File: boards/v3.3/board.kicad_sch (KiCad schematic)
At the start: 61 parts, among them J1 KF301-2P, J2 KF301-2P, J3 KF301-2P, J4 KF301-2P, J5 KF301-2P, J6 KF301-2P, P1 Pin Header, P2 Pin Header, P3 Pin Header, P4 Pin Header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

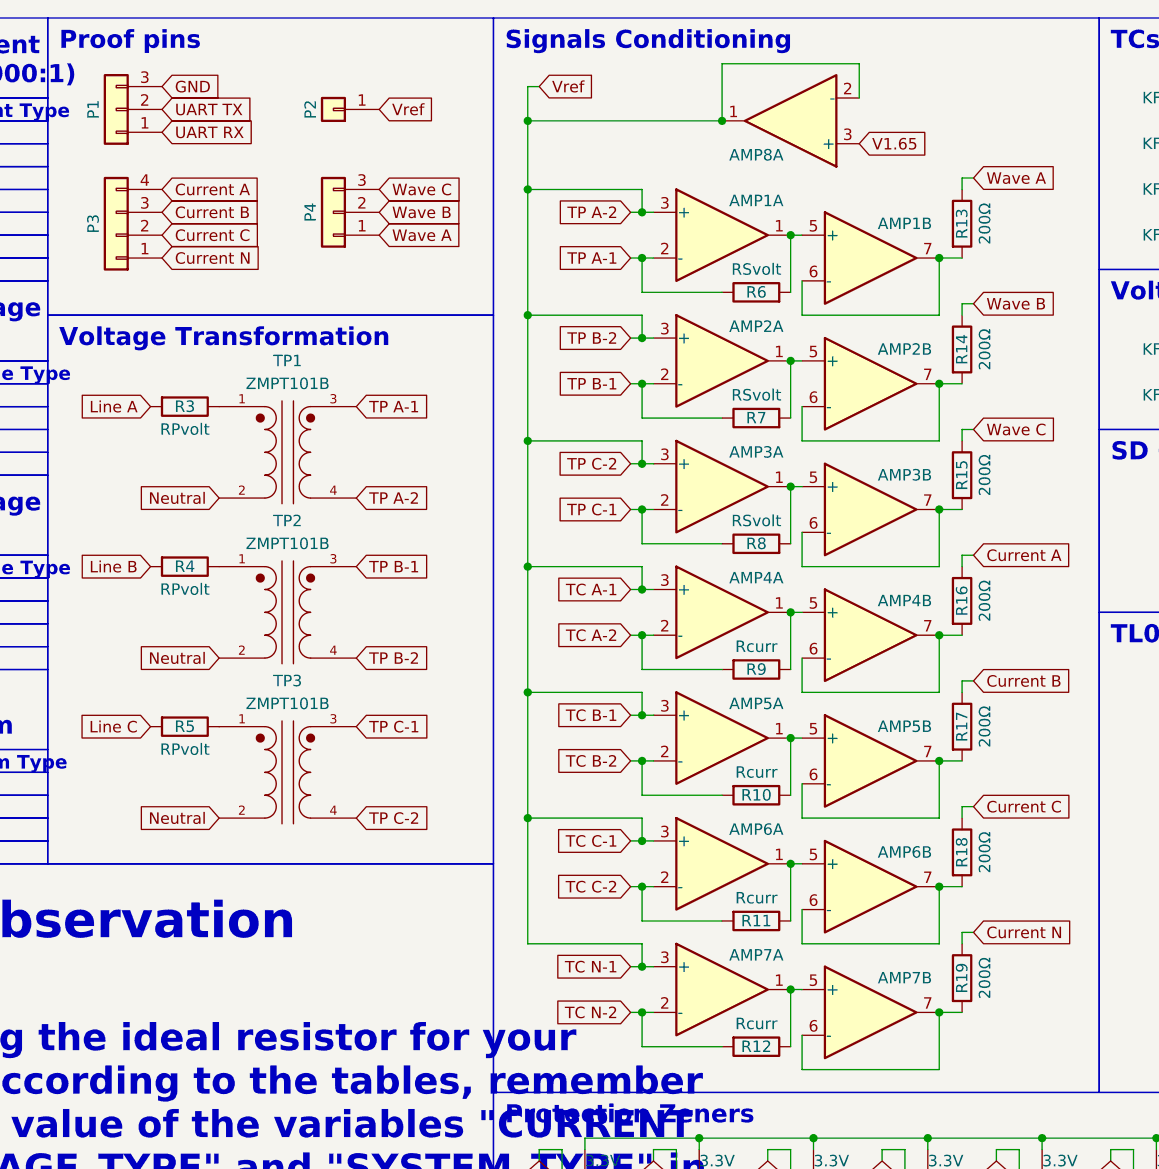
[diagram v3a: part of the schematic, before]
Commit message: Recalculation of load resistors
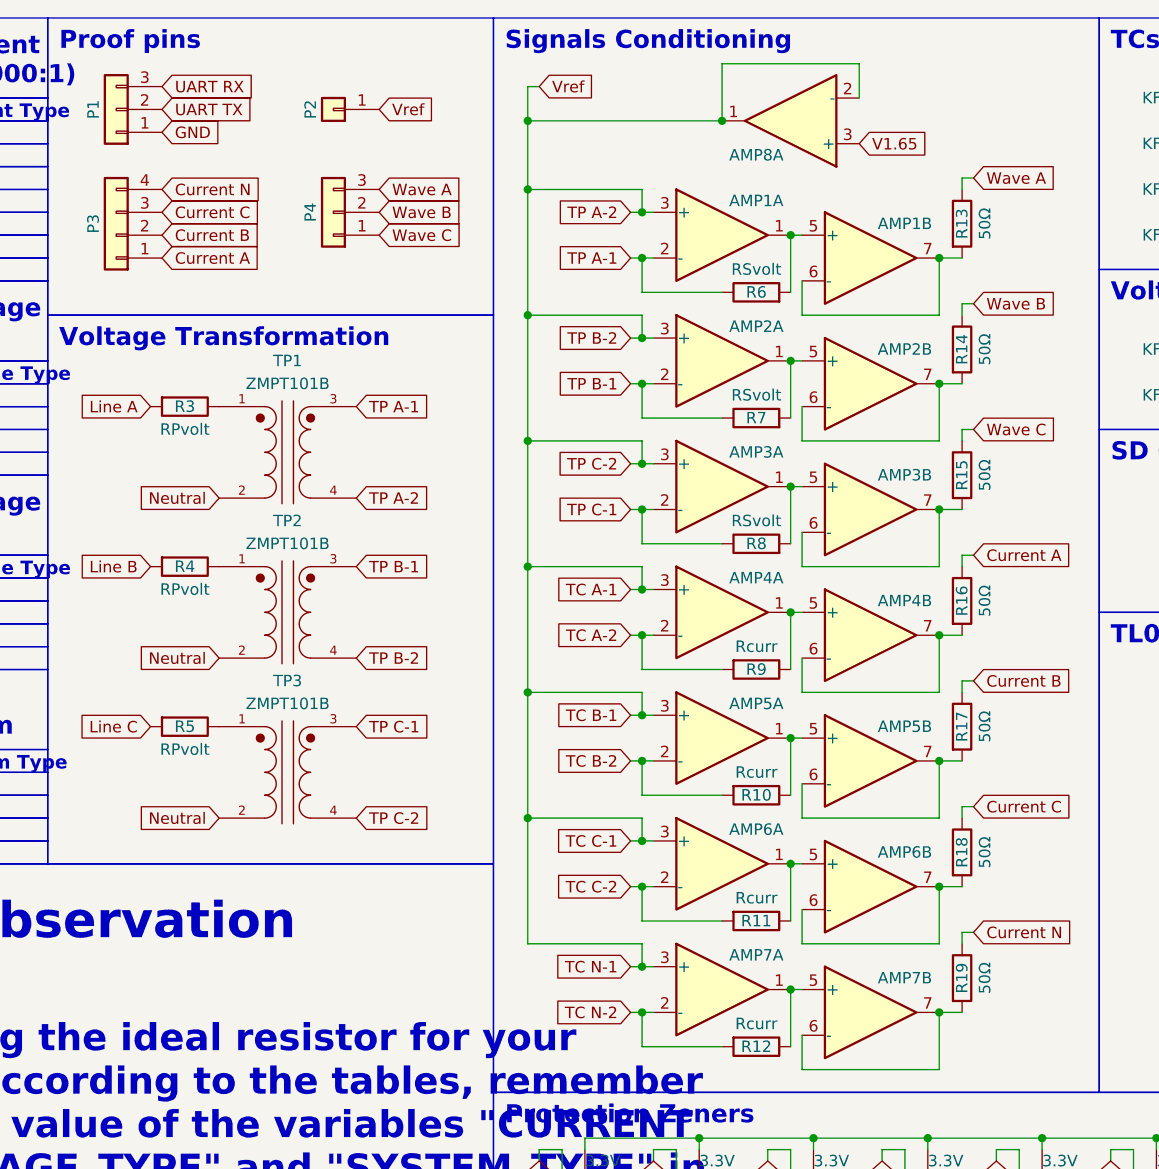
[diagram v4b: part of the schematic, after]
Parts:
- R13, R14, R15, R16, R17, R18, R19: value 200Ω -> 50Ω
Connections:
- net Current A: now also P3.1 (Pin_1); no longer P3.4 (Pin_4)
- net Current B: now also P3.2 (Pin_2); no longer P3.3 (Pin_3)
- net Current C: now also P3.3 (Pin_3); no longer P3.2 (Pin_2)
- net Current N: now also P3.4 (Pin_4); no longer P3.1 (Pin_1)
- net GND: now also P1.1 (Pin_1); no longer P1.3 (Pin_3)
- net UART RX: now also P1.3 (Pin_3); no longer P1.1 (Pin_1)
- net Wave A: now also P4.3 (Pin_3); no longer P4.1 (Pin_1)
- net Wave C: now also P4.1 (Pin_1); no longer P4.3 (Pin_3)
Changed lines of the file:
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@@
     (title "Power Vision V3.3 Schematic")
     (date "02/06/2024")
-    (rev "1.3")
+    (rev "1.4")
     (company "linkedin.com/in/lucasrguerra")
     (comment 1 "github.com/lucasrguerra/power_vision")
@@
     )
   )
-  (global_label "GND" (shape input) (at 68.58 21.59 0) (fields_autoplaced)
-    (effects (font (size 1.27 1.27)) (justify left))
-    (property "Intersheetrefs" "${INTERSHEET_REFS}" (at 75.4357 21.59 0)
-      (effects (font (size 1.27 1.27)) (justify left) hide)
-    )
-  )
   (global_label "Neutral" (shape input) (at 194.31 48.26 0) (fields_autoplaced)
     (effects (font (size 1.27 1.27)) (justify left))
@@
     )
   )
+  (global_label "Wave A" (shape input) (at 92.71 33.02 0) (fields_autoplaced)
+    (effects (font (size 1.27 1.27)) (justify left))
+    (property "Intersheetrefs" "${INTERSHEET_REFS}" (at 102.408 33.02 0)
+      (effects (font (size 1.27 1.27)) (justify left) hide)
+    )
+  )
   (global_label "TC A-2" (shape input) (at 120.65 82.55 180) (fields_autoplaced)
     (effects (font (size 1.27 1.27)) (justify right))
@@
     )
   )
-  (global_label "Current N" (shape input) (at 68.58 40.64 0) (fields_autoplaced)
-    (effects (font (size 1.27 1.27)) (justify left))
-    (property "Intersheetrefs" "${INTERSHEET_REFS}" (at 80.818 40.64 0)
-      (effects (font (size 1.27 1.27)) (justify left) hide)
-    )
-  )
   (global_label "Current A" (shape input) (at 158.75 73.66 0) (fields_autoplaced)
     (effects (font (size 1.27 1.27)) (justify left))
@@
     )
   )
-  (global_label "UART RX" (shape input) (at 68.58 26.67 0) (fields_autoplaced)
-    (effects (font (size 1.27 1.27)) (justify left))
-    (property "Intersheetrefs" "${INTERSHEET_REFS}" (at 79.669 26.67 0)
-      (effects (font (size 1.27 1.27)) (justify left) hide)
-    )
-  )
   (global_label "TC B-1" (shape input) (at 194.31 25.4 0) (fields_autoplaced)
     (effects (font (size 1.27 1.27)) (justify left))
@@
     )
   )
+  (global_label "UART TX" (shape input) (at 68.58 24.13 0) (fields_autoplaced)
+    (effects (font (size 1.27 1.27)) (justify left))
+    (property "Intersheetrefs" "${INTERSHEET_REFS}" (at 79.3666 24.13 0)
+      (effects (font (size 1.27 1.27)) (justify left) hide)
+    )
+  )
   (global_label "TP B-1" (shape input) (at 120.65 54.61 180) (fields_autoplaced)
     (effects (font (size 1.27 1.27)) (justify right))
@@
     )
   )
-  (global_label "Current B" (shape input) (at 68.58 35.56 0) (fields_autoplaced)
-    (effects (font (size 1.27 1.27)) (justify left))
-    (property "Intersheetrefs" "${INTERSHEET_REFS}" (at 80.7575 35.56 0)
-      (effects (font (size 1.27 1.27)) (justify left) hide)
-    )
-  )
   (global_label "Wave B" (shape input) (at 158.75 45.72 0) (fields_autoplaced)
     (effects (font (size 1.27 1.27)) (justify left))
@@
     )
   )
-  (global_label "TP C-1" (shape input) (at 120.65 68.58 180) (fields_autoplaced)
-    (effects (font (size 1.27 1.27)) (justify right))
-    (property "Intersheetrefs" "${INTERSHEET_REFS}" (at 110.4077 68.58 0)
-      (effects (font (size 1.27 1.27)) (justify right) hide)
-    )
-  )
-  (global_label "Current A" (shape input) (at 68.58 33.02 0) (fields_autoplaced)
+  (global_label "Current N" (shape input) (at 68.58 33.02 0) (fields_autoplaced)
     (effects (font (size 1.27 1.27)) (justify left))
-    (property "Intersheetrefs" "${INTERSHEET_REFS}" (at 80.5761 33.02 0)
+    (property "Intersheetrefs" "${INTERSHEET_REFS}" (at 80.818 33.02 0)
       (effects (font (size 1.27 1.27)) (justify left) hide)
     )
   )
-  (global_label "Wave C" (shape input) (at 92.71 33.02 0) (fields_autoplaced)
-    (effects (font (size 1.27 1.27)) (justify left))
-    (property "Intersheetrefs" "${INTERSHEET_REFS}" (at 102.5894 33.02 0)
-      (effects (font (size 1.27 1.27)) (justify left) hide)
+  (global_label "TP C-1" (shape input) (at 120.65 68.58 180) (fields_autoplaced)
+    (effects (font (size 1.27 1.27)) (justify right))
+    (property "Intersheetrefs" "${INTERSHEET_REFS}" (at 110.4077 68.58 0)
+      (effects (font (size 1.27 1.27)) (justify right) hide)
     )
   )
@@
     )
   )
+  (global_label "UART RX" (shape input) (at 68.58 21.59 0) (fields_autoplaced)
+    (effects (font (size 1.27 1.27)) (justify left))
+    (property "Intersheetrefs" "${INTERSHEET_REFS}" (at 79.669 21.59 0)
+      (effects (font (size 1.27 1.27)) (justify left) hide)
+    )
+  )
   (global_label "V1.65" (shape input) (at 271.78 152.4 0) (fields_autoplaced)
     (effects (font (size 1.27 1.27)) (justify left))
@@
     )
   )
+  (global_label "Current A" (shape input) (at 68.58 40.64 0) (fields_autoplaced)
+    (effects (font (size 1.27 1.27)) (justify left))
+    (property "Intersheetrefs" "${INTERSHEET_REFS}" (at 80.5761 40.64 0)
+      (effects (font (size 1.27 1.27)) (justify left) hide)
+    )
+  )
   (global_label "TC A-1" (shape input) (at 120.65 77.47 180) (fields_autoplaced)
     (effects (font (size 1.27 1.27)) (justify right))
@@
     )
   )
-  (global_label "Wave B" (shape input) (at 92.71 35.56 0) (fields_autoplaced)
-    (effects (font (size 1.27 1.27)) (justify left))
-    (property "Intersheetrefs" "${INTERSHEET_REFS}" (at 102.5894 35.56 0)
-      (effects (font (size 1.27 1.27)) (justify left) hide)
-    )
-  )
   (global_label "TC C-1" (shape input) (at 194.31 30.48 0) (fields_autoplaced)
     (effects (font (size 1.27 1.27)) (justify left))
@@
     )
   )
+  (global_label "Wave B" (shape input) (at 92.71 35.56 0) (fields_autoplaced)
+    (effects (font (size 1.27 1.27)) (justify left))
+    (property "Intersheetrefs" "${INTERSHEET_REFS}" (at 102.5894 35.56 0)
+      (effects (font (size 1.27 1.27)) (justify left) hide)
+    )
+  )
   (global_label "GND" (shape input) (at 196.85 69.85 90) (fields_autoplaced)
     (effects (font (size 1.27 1.27)) (justify left))
@@
     )
   )
+  (global_label "Current C" (shape input) (at 68.58 35.56 0) (fields_autoplaced)
+    (effects (font (size 1.27 1.27)) (justify left))
+    (property "Intersheetrefs" "${INTERSHEET_REFS}" (at 80.7575 35.56 0)
+      (effects (font (size 1.27 1.27)) (justify left) hide)
+    )
+  )
   (global_label "TC N-1" (shape input) (at 120.65 119.38 180) (fields_autoplaced)
     (effects (font (size 1.27 1.27)) (justify right))
@@
     )
   )
+  (global_label "GND" (shape input) (at 68.58 26.67 0) (fields_autoplaced)
+    (effects (font (size 1.27 1.27)) (justify left))
+    (property "Intersheetrefs" "${INTERSHEET_REFS}" (at 75.4357 26.67 0)
+      (effects (font (size 1.27 1.27)) (justify left) hide)
+    )
+  )
   (global_label "TP B-1" (shape input) (at 90.17 74.93 0) (fields_autoplaced)
     (effects (font (size 1.27 1.27)) (justify left))
@@
     )
   )
-  (global_label "UART TX" (shape input) (at 68.58 24.13 0) (fields_autoplaced)
-    (effects (font (size 1.27 1.27)) (justify left))
-    (property "Intersheetrefs" "${INTERSHEET_REFS}" (at 79.3666 24.13 0)
-      (effects (font (size 1.27 1.27)) (justify left) hide)
-    )
-  )
   (global_label "Line A" (shape input) (at 194.31 55.88 0) (fields_autoplaced)
     (effects (font (size 1.27 1.27)) (justify left))
@@
     )
   )
-  (global_label "Current C" (shape input) (at 68.58 38.1 0) (fields_autoplaced)
+  (global_label "Current B" (shape input) (at 68.58 38.1 0) (fields_autoplaced)
     (effects (font (size 1.27 1.27)) (justify left))
     (property "Intersheetrefs" "${INTERSHEET_REFS}" (at 80.7575 38.1 0)
@@
     )
   )
+  (global_label "Wave C" (shape input) (at 92.71 38.1 0) (fields_autoplaced)
+    (effects (font (size 1.27 1.27)) (justify left))
+    (property "Intersheetrefs" "${INTERSHEET_REFS}" (at 102.5894 38.1 0)
+      (effects (font (size 1.27 1.27)) (justify left) hide)
+    )
+  )
   (global_label "Current B" (shape input) (at 161.29 140.97 270) (fields_autoplaced)
     (effects (font (size 1.27 1.27)) (justify right))
@@
     )
   )
-  (global_label "Wave A" (shape input) (at 92.71 38.1 0) (fields_autoplaced)
-    (effects (font (size 1.27 1.27)) (justify left))
-    (property "Intersheetrefs" "${INTERSHEET_REFS}" (at 102.408 38.1 0)
-      (effects (font (size 1.27 1.27)) (justify left) hide)
-    )
-  )
   (global_label "TP C-1" (shape input) (at 90.17 92.71 0) (fields_autoplaced)
     (effects (font (size 1.27 1.27)) (justify left))
@@
       (effects (font (size 1.27 1.27)))
     )
-    (property "Value" "200Ω" (at 160.02 106.68 90)
+    (property "Value" "50Ω" (at 160.02 106.68 90)
       (effects (font (size 1.27 1.27)))
     )
@@
       (effects (font (size 1.27 1.27)))
     )
-    (property "Value" "200Ω" (at 160.02 36.83 90)
+    (property "Value" "50Ω" (at 160.02 36.83 90)
       (effects (font (size 1.27 1.27)))
     )
@@
       (effects (font (size 1.27 1.27)))
     )
-    (property "Value" "200Ω" (at 160.02 78.74 90)
+    (property "Value" "50Ω" (at 160.02 78.74 90)
       (effects (font (size 1.27 1.27)))
     )
@@
       (effects (font (size 1.27 1.27)))
     )
-    (property "Value" "200Ω" (at 160.02 50.8 90)
+    (property "Value" "50Ω" (at 160.02 50.8 90)
       (effects (font (size 1.27 1.27)))
     )
@@
       (effects (font (size 1.27 1.27)))
     )
-    (property "Value" "200Ω" (at 160.02 92.71 90)
+    (property "Value" "50Ω" (at 160.02 92.71 90)
       (effects (font (size 1.27 1.27)))
     )
@@
       (effects (font (size 1.27 1.27)))
     )
-    (property "Value" "200Ω" (at 160.02 120.65 90)
+    (property "Value" "50Ω" (at 160.02 120.65 90)
       (effects (font (size 1.27 1.27)))
     )
@@
       (effects (font (size 1.27 1.27)))
     )
-    (property "Value" "200Ω" (at 160.02 64.77 90)
+    (property "Value" "50Ω" (at 160.02 64.77 90)
       (effects (font (size 1.27 1.27)))
     )

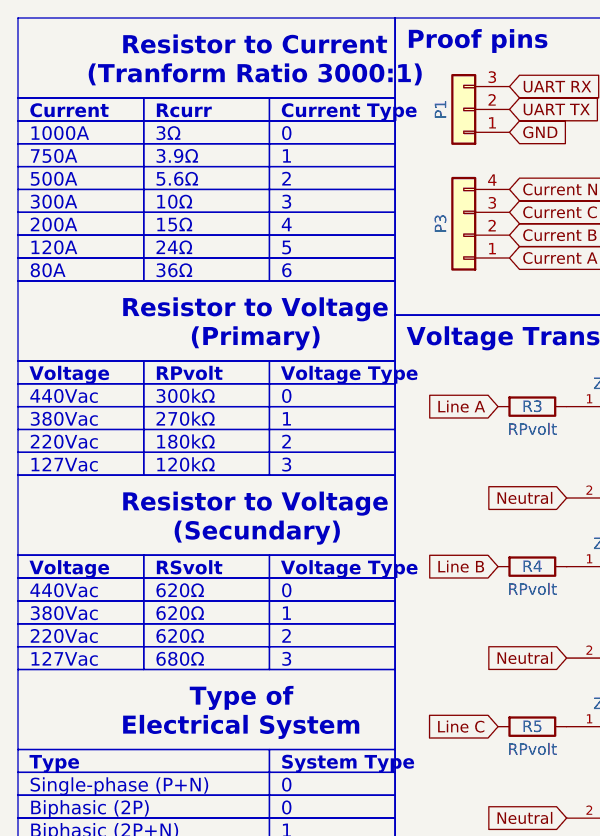
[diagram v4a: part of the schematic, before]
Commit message: Update and correct calcs of the signals
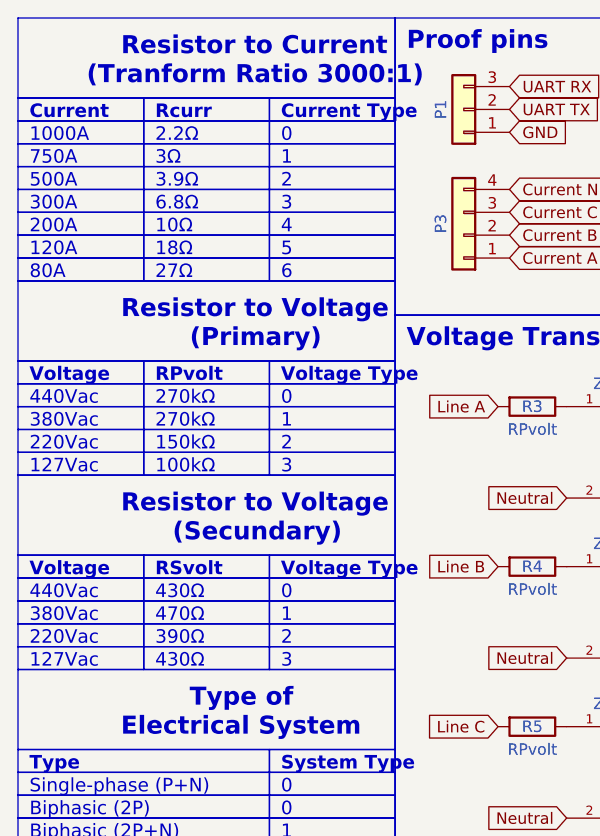
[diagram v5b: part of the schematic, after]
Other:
- note added: "100kΩ"
- note added: "150kΩ"
- note added: "18Ω"
- note added: "2.2Ω"
- note added: "27Ω"
- note added: "390Ω"
- note added: "430Ω"
- note added: "470Ω"
- note added: "6.8Ω"
- note removed: "120kΩ"
- note removed: "15Ω"
- note removed: "180kΩ"
- note removed: "24Ω"
- note removed: "300kΩ"
- note removed: "36Ω"
- note removed: "5.6Ω"
- note removed: "620Ω"
- note removed: "680Ω"
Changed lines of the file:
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@@
   (title_block
     (title "Power Vision V3.3 Schematic")
-    (date "02/06/2024")
-    (rev "1.4")
+    (date "04/06/2024")
+    (rev "1.5")
     (company "linkedin.com/in/lucasrguerra")
     (comment 1 "github.com/lucasrguerra/power_vision")
@@
     (effects (font (face "Calibri") (size 1.5 1.5)) (justify left bottom))
   )
-  (text "36Ω" (at 29.21 43.18 0)
+  (text "27Ω" (at 29.21 43.18 0)
     (effects (font (face "Calibri") (size 1.5 1.5)) (justify left bottom))
   )
@@
     (effects (font (face "Calibri") (size 1.5 1.5) (thickness 0.3) bold) (justify left bottom))
   )
-  (text "15Ω" (at 29.21 38.1 0)
+  (text "10Ω" (at 29.21 38.1 0)
     (effects (font (face "Calibri") (size 1.5 1.5)) (justify left bottom))
   )
@@
     (effects (font (face "Calibri") (size 1.5 1.5)) (justify left bottom))
   )
-  (text "620Ω" (at 29.21 81.28 0)
+  (text "470Ω" (at 29.21 81.28 0)
     (effects (font (face "Calibri") (size 1.5 1.5)) (justify left bottom))
   )
@@
     (effects (font (face "Calibri") (size 2 2) (thickness 0.254) bold) (justify left bottom))
   )
-  (text "3.9Ω" (at 29.21 30.48 0)
+  (text "3Ω" (at 29.21 30.48 0)
     (effects (font (face "Calibri") (size 1.5 1.5)) (justify left bottom))
   )
@@
     (effects (font (face "Calibri") (size 1.5 1.5)) (justify left bottom))
   )
-  (text "5.6Ω" (at 29.21 33.02 0)
+  (text "3.9Ω" (at 29.21 33.02 0)
     (effects (font (face "Calibri") (size 1.5 1.5)) (justify left bottom))
   )
@@
     (effects (font (face "Calibri") (size 2 2) (thickness 0.254) bold) (justify left bottom))
   )
-  (text "300kΩ" (at 29.21 57.15 0)
+  (text "270kΩ" (at 29.21 57.15 0)
     (effects (font (face "Calibri") (size 1.5 1.5)) (justify left bottom))
   )
@@
     (effects (font (face "Calibri") (size 1.5 1.5)) (justify left bottom))
   )
-  (text "120kΩ" (at 29.21 64.77 0)
+  (text "100kΩ" (at 29.21 64.77 0)
     (effects (font (face "Calibri") (size 1.5 1.5)) (justify left bottom))
   )
@@
     (effects (font (face "Calibri") (size 1.5 1.5)) (justify left bottom))
   )
-  (text "24Ω" (at 29.21 40.64 0)
-    (effects (font (face "Calibri") (size 1.5 1.5)) (justify left bottom))
-  )
-  (text "10Ω" (at 29.21 35.56 0)
-    (effects (font (face "Calibri") (size 1.5 1.5)) (justify left bottom))
-  )
-  (text "620Ω" (at 29.21 83.82 0)
+  (text "18Ω" (at 29.21 40.64 0)
+    (effects (font (face "Calibri") (size 1.5 1.5)) (justify left bottom))
+  )
+  (text "6.8Ω" (at 29.21 35.56 0)
+    (effects (font (face "Calibri") (size 1.5 1.5)) (justify left bottom))
+  )
+  (text "390Ω" (at 29.21 83.82 0)
     (effects (font (face "Calibri") (size 1.5 1.5)) (justify left bottom))
   )
@@
     (effects (font (face "Calibri") (size 1.5 1.5)) (justify left bottom))
   )
-  (text "180kΩ" (at 29.21 62.23 0)
+  (text "150kΩ" (at 29.21 62.23 0)
     (effects (font (face "Calibri") (size 1.5 1.5)) (justify left bottom))
   )
@@
     (effects (font (face "Calibri") (size 1.5 1.5)) (justify left bottom))
   )
-  (text "680Ω" (at 29.21 86.36 0)
+  (text "430Ω" (at 29.21 86.36 0)
     (effects (font (face "Calibri") (size 1.5 1.5)) (justify left bottom))
   )
@@
     (effects (font (face "Calibri") (size 1.5 1.5) (thickness 0.3) bold) (justify left bottom))
   )
-  (text "3Ω" (at 29.21 27.94 0)
+  (text "2.2Ω" (at 29.21 27.94 0)
     (effects (font (face "Calibri") (size 1.5 1.5)) (justify left bottom))
   )
@@
     (effects (font (face "Calibri") (size 1.5 1.5)) (justify left bottom))
   )
-  (text "620Ω" (at 29.21 78.74 0)
-    (effects (font (face "Calibri") (size 1.5 1.5)) (justify left bottom))
-  )
+  (text "430Ω" (at 29.21 78.74 0)
+    (effects (font (face "Calibri") (size 1.5 1.5)) (justify left bottom))
+  )
